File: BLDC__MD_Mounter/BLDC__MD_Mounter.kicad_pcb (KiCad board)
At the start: 2 copper layers, 14 parts, among them J1 Conn_02x07_Odd_Even, J10 Conn_02x07_Odd_Even, J11 Conn_01x08_Female, J12 Conn_02x07_Odd_Even, J13 Conn_02x07_Odd_Even, J14 Conn_01x08_Female, J2 Conn_02x07_Odd_Even, J3 Conn_02x10_Odd_Even, J4 Conn_01x08_Female, J5 Conn_01x02_Male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

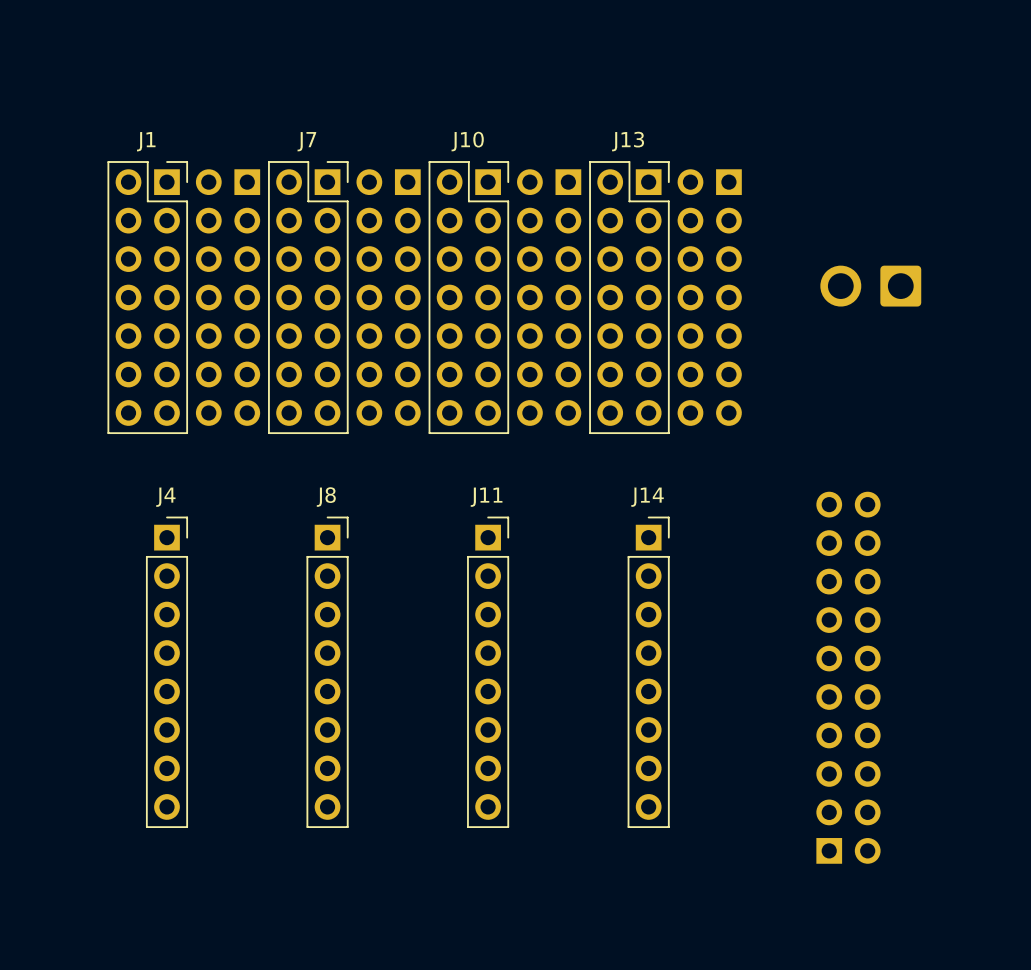
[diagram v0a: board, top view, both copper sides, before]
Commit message: Connected some simple lines
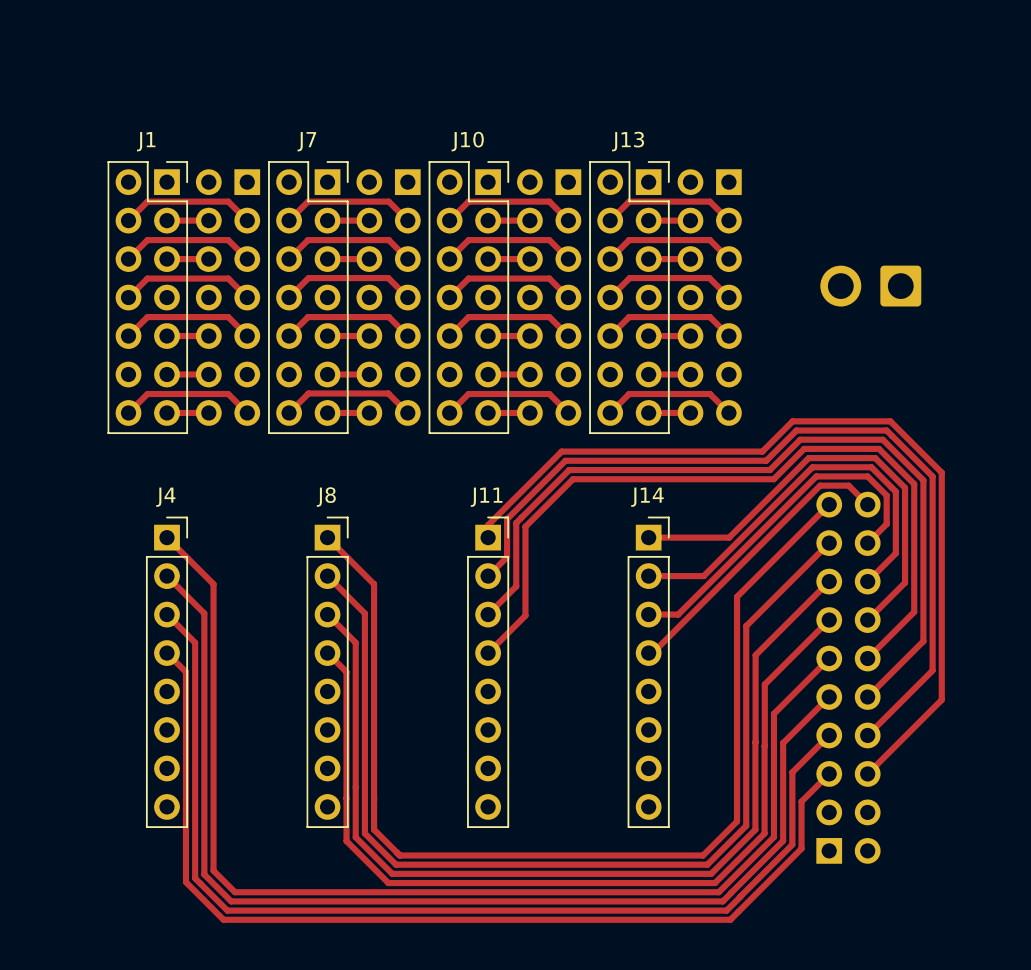
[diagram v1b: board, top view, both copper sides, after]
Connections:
- J3 pad 10: /PWM_4 -> /PWM_3
- J3 pad 12: /RD_4 -> /RD_3
- J3 pad 14: /FG_3 -> /FG_4
- J3 pad 16: /FR_3 -> /FR_4
- J3 pad 18: /PWM_3 -> /PWM_4
- J3 pad 20: /RD_3 -> /RD_4
- J3 pad 6: /FG_4 -> /FG_3
- J3 pad 8: /FR_4 -> /FR_3
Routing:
- net /FG_1: track 0.00 -> 75.7 mm
- net /FR_1: track 0.00 -> 72.1 mm
- net /FG_2: track 0.00 -> 70.1 mm
- net /PWM_1: track 0.00 -> 68.5 mm
- net /FR_2: track 0.00 -> 66.0 mm
- net /RD_1: track 0.00 -> 65.0 mm
- net /PWM_2: track 0.00 -> 62.5 mm
- net /RD_2: track 0.00 -> 58.9 mm
- net /FG_3: track 0.00 -> 56.9 mm
- net /FR_3: track 0.00 -> 54.9 mm
- net /PWM_3: track 0.00 -> 52.9 mm
- net /RD_3: track 0.00 -> 50.9 mm
- net /FG_4: track 0.00 -> 29.7 mm
- net /FR_4: track 0.00 -> 26.7 mm
- net /PWM_4: track 0.00 -> 23.7 mm
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
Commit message: Connected all components. And exported CAD files.
The CAD file type is .step and there are two pictures of the board, front and back.
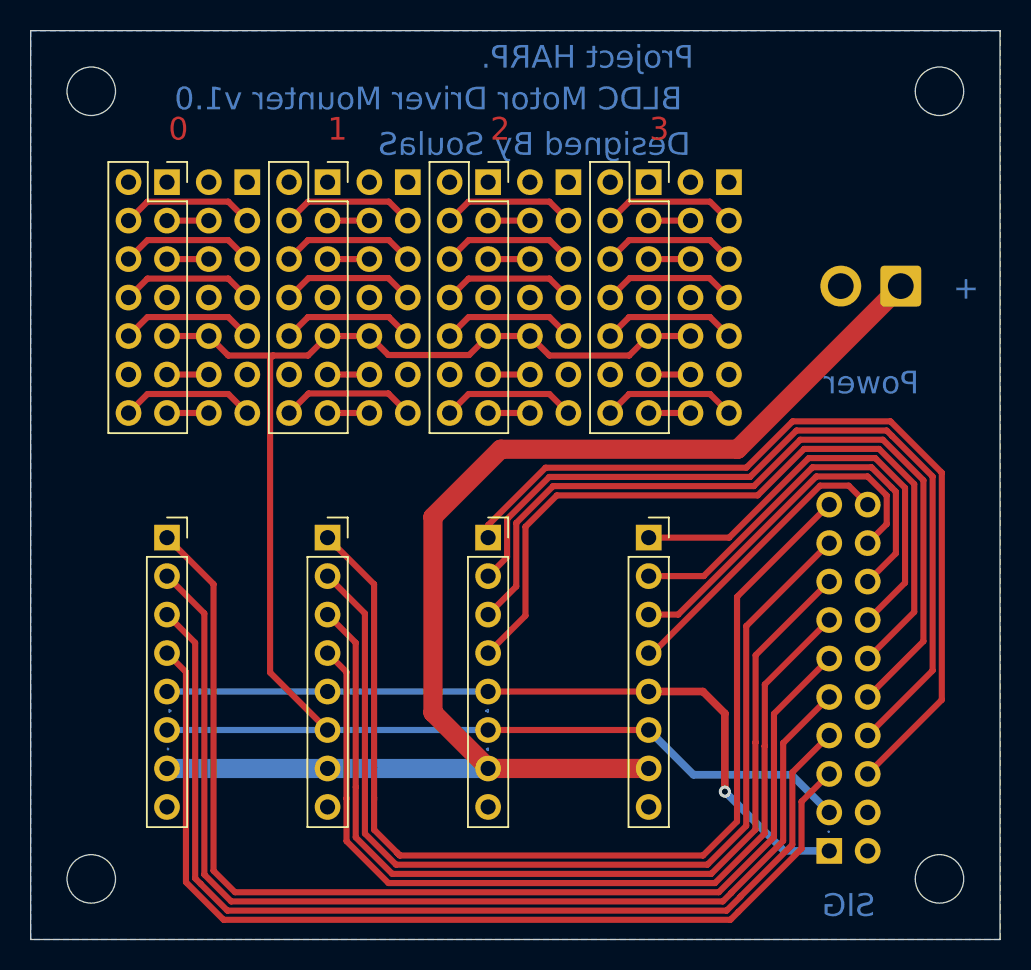
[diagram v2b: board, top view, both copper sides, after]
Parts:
- added REF**: MountingHole_3.2mm_M3, MountingHole:MountingHole_3.2mm_M3, F.Cu at (161.0, 113.0)
- added REF**: MountingHole_3.2mm_M3, MountingHole:MountingHole_3.2mm_M3, F.Cu at (161.0, 61.0)
- added REF**: MountingHole_3.2mm_M3, MountingHole:MountingHole_3.2mm_M3, F.Cu at (105.0, 61.0)
- added REF**: MountingHole_3.2mm_M3, MountingHole:MountingHole_3.2mm_M3, F.Cu at (105.0, 113.0)
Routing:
- net +5V: track 11.0 -> 110.1 mm
- net VCC: track 0.00 -> 87.1 mm
- net +3V3: track 0.00 -> 51.1 mm, vias 0 -> 1
- added copper zone on B.Cu, net GND
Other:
- board outline added: 64 x 60 mm
- board text added: "+"
- board text added: "0"
- board text added: "1"
- board text added: "2"
- board text added: "3"
- board text added: "BLDC Motor Driver Mounter v1.0"
- board text added: "Designed By SoulaS"
- board text added: "Power"
- board text added: "Project HARP."
- board text added: "SIG"

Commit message: Fixed the location of the single line pinheader bottom side of the board.
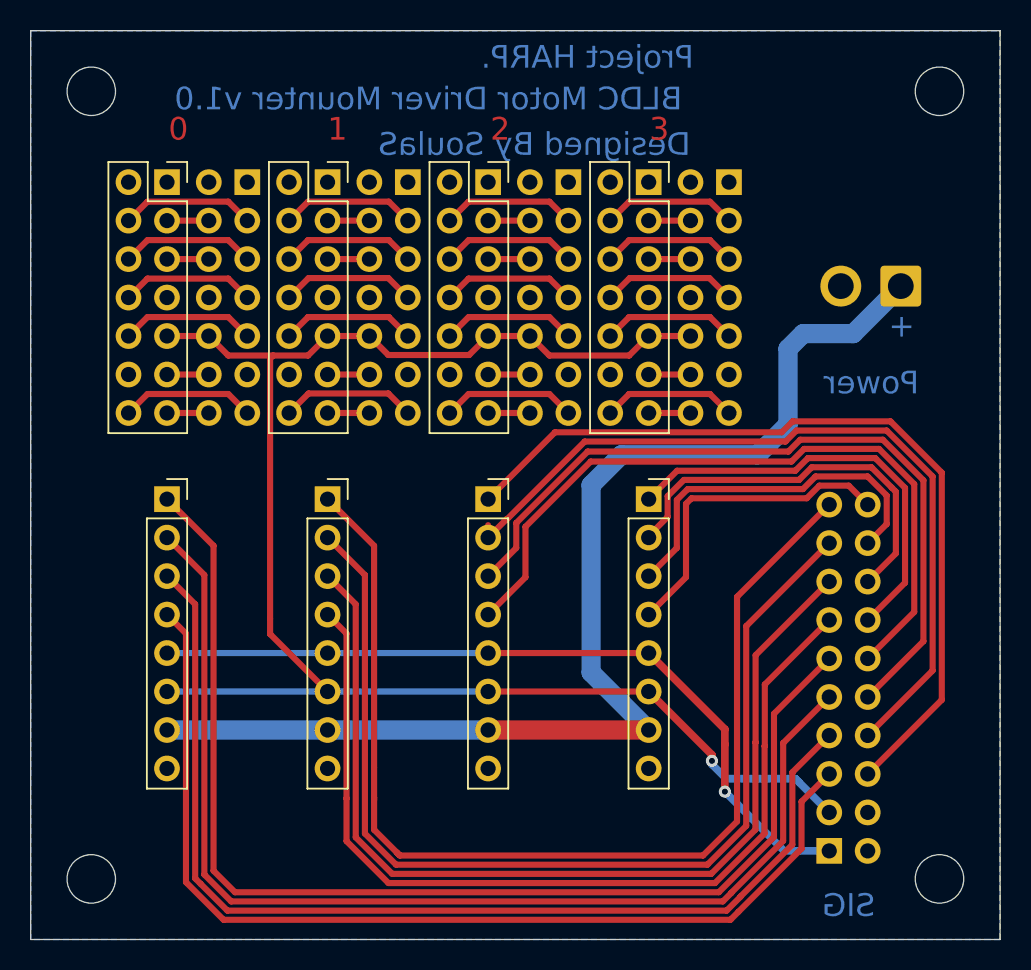
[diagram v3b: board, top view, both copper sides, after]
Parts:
- moved J11 2.54 mm to (131.2, 87.9)
- moved J14 2.54 mm to (141.8, 87.9)
- moved J4 2.54 mm to (110.0, 87.9)
- moved J8 2.54 mm to (120.6, 87.9)
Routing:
- net VCC: track 87.1 -> 78.4 mm
- net /FR_2: track 66.0 -> 68.6 mm
- net /FR_1: track 72.1 -> 74.6 mm
- net /RD_2: track 58.9 -> 61.4 mm
- net /RD_3: track 50.9 -> 48.4 mm
- net /FG_1: track 75.7 -> 78.2 mm
- net /RD_1: track 65.0 -> 67.5 mm
- net /PWM_1: track 68.5 -> 71.1 mm
- net /FG_2: track 70.1 -> 72.6 mm
- net /PWM_2: track 62.5 -> 65.0 mm
- net /PWM_3: track 52.9 -> 50.4 mm
- net /RD_4: track 19.6 -> 21.3 mm
- net /FR_3: track 54.9 -> 53.2 mm
- net /FG_3: track 56.9 -> 55.4 mm
- net +5V: track 110.1 -> 109.0 mm, vias 0 -> 1
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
